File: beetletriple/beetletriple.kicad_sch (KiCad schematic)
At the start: 1 part, among them J1 Power IN

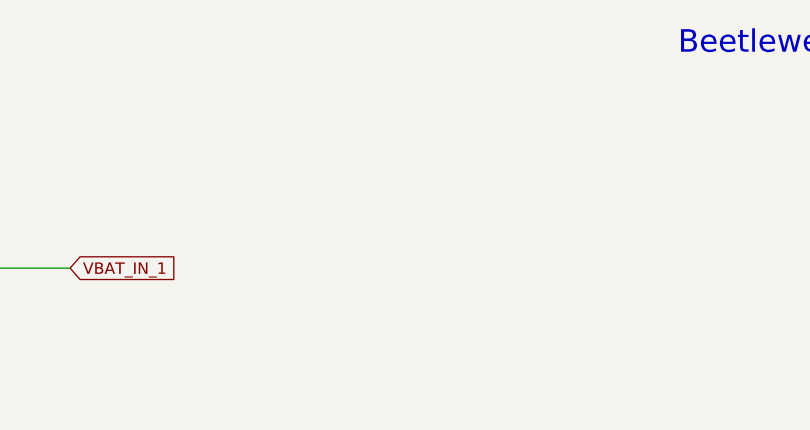
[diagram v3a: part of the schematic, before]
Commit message: Pin swaps and routing
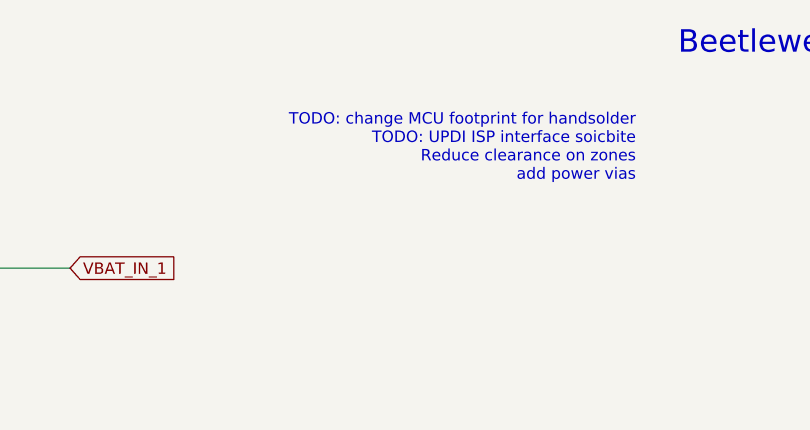
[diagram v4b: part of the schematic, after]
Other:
- note added: "TODO: change MCU footprint for handsolder TODO: UPDI ISP interface soicbite Reduce clearance on zones add power vias"
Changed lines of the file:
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@@
     (stroke (width 0) (type solid) (color 0 0 0 0))
+  )
+  (text "TODO: change MCU footprint for handsolder\nTODO: UPDI ISP interface soicbite\nReduce clearance on zones\nadd power vias "
+    (at 109.22 43.815 0)
+    (effects (font (size 1.27 1.27)) (justify right bottom))
   )
   (text "Beetleweight triple ESC" (at 154.305 29.845 180)
@@
       (reference "J1") (unit 1) (value "Power IN") (footprint "TerminalBlock:TerminalBlock_Wuerth_691311400102_P7.62mm")
     )
+    (path "/6d93a432-011d-4d1d-9c43-a648615a7ea3/22d9c911-bea7-4fc4-93b7-a8a13fd1aa13"
+      (reference "#FLG0101") (unit 1) (value "PWR_FLAG") (footprint "")
+    )
+    (path "/6d93a432-011d-4d1d-9c43-a648615a7ea3/75b3d201-a388-4172-8517-0aab374793dc"
+      (reference "#FLG0102") (unit 1) (value "PWR_FLAG") (footprint "")
+    )
+    (path "/6d93a432-011d-4d1d-9c43-a648615a7ea3/b538e895-f3c3-446e-9001-2df4142c87bf"
+      (reference "#FLG?") (unit 1) (value "PWR_FLAG") (footprint "")
+    )
     (path "/6d93a432-011d-4d1d-9c43-a648615a7ea3/60cf72a3-da49-4391-a543-e025e0f19f60"

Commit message: Add new power in connector
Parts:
- J1: footprint TerminalBlock:TerminalBlock_Wuerth_691311400102_P7.62mm -> beetletriple:beetlepower
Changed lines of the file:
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@@
     (property "Reference" "J1" (id 0) (at 27.4574 47.7582 0))
     (property "Value" "Power IN" (id 1) (at 27.4574 50.0569 0))
-    (property "Footprint" "TerminalBlock:TerminalBlock_Wuerth_691311400102_P7.62mm" (id 2) (at 24.765 55.88 0)
+    (property "Footprint" "beetletriple:beetlepower" (id 2) (at 24.765 55.88 0)
       (effects (font (size 1.27 1.27)) hide)
     )
@@
     )
     (path "/9e85b9a1-64a3-43d7-a600-53fc362386e6"
-      (reference "J1") (unit 1) (value "Power IN") (footprint "TerminalBlock:TerminalBlock_Wuerth_691311400102_P7.62mm")
+      (reference "J1") (unit 1) (value "Power IN") (footprint "beetletriple:beetlepower")
     )
     (path "/6d93a432-011d-4d1d-9c43-a648615a7ea3/22d9c911-bea7-4fc4-93b7-a8a13fd1aa13"

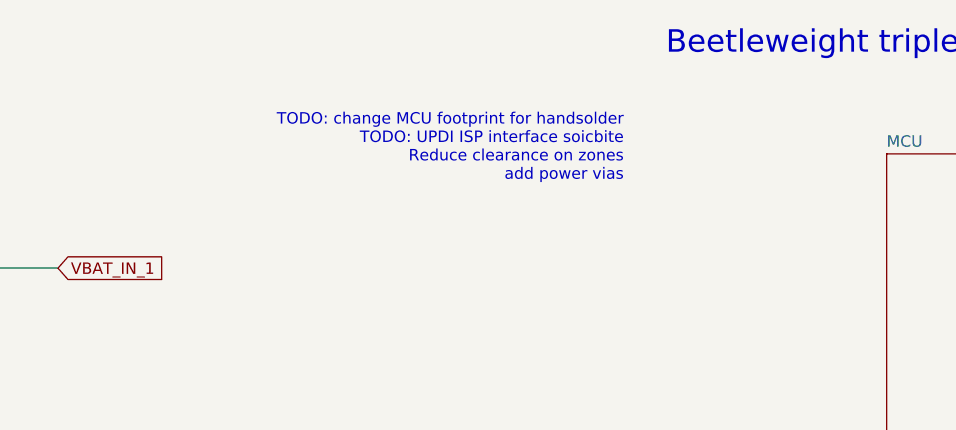
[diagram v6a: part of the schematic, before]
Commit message: Shunt current sensor. Many improvements, layout updates
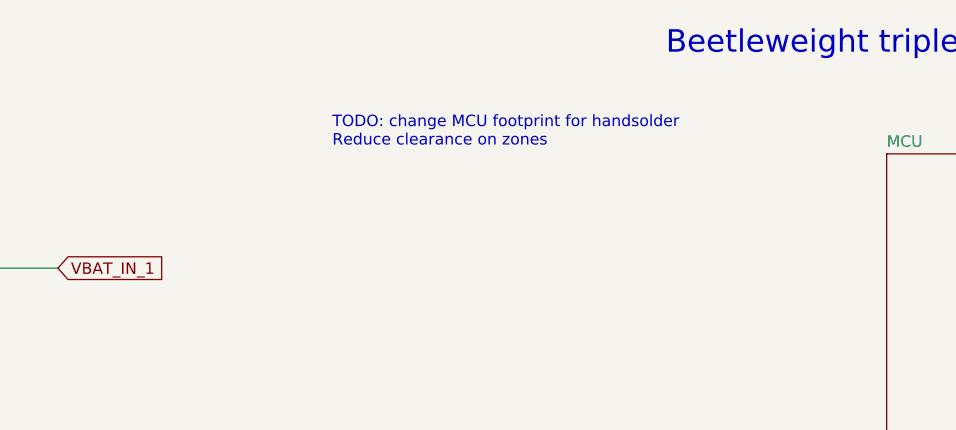
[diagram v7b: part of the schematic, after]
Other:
- note added: "TODO: change MCU footprint for handsolder Reduce clearance on zones"
- note removed: "TODO: change MCU footprint for handsolder TODO: UPDI ISP interface soicbite Reduce clearance on zones add power vias"
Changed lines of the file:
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@@
     (stroke (width 0) (type solid) (color 0 0 0 0))
   )
-  (text "TODO: change MCU footprint for handsolder\nTODO: UPDI ISP interface soicbite\nReduce clearance on zones\nadd power vias "
-    (at 109.22 43.815 0)
-    (effects (font (size 1.27 1.27)) (justify right bottom))
+  (text "TODO: change MCU footprint for handsolder\nReduce clearance on zones\n"
+    (at 76.835 40.005 0)
+    (effects (font (size 1.27 1.27)) (justify left bottom))
   )
   (text "Beetleweight triple ESC" (at 154.305 29.845 180)
@@
     )
     (path "/6d93a432-011d-4d1d-9c43-a648615a7ea3/f69d8565-9cce-4269-8146-6fce66bbe553"
-      (reference "F1") (unit 1) (value "20mmx5 fuse holder") (footprint "Fuse:Fuseholder_Cylinder-5x20mm_Schurter_0031_8201_Horizontal_Open")
+      (reference "F1") (unit 1) (value "20mmx5 fuse holder") (footprint "beetletriple:fuseholder_flexible")
     )
     (path "/6d93a432-011d-4d1d-9c43-a648615a7ea3/867e4d9b-1a41-4ccb-b503-ce8c72df462b"
@@
       (reference "U3") (unit 1) (value "ATtiny1617-M") (footprint "Package_DFN_QFN:QFN-24-1EP_4x4mm_P0.5mm_EP2.6x2.6mm")
     )
-    (path "/88009e22-8327-4e67-a142-0e1ef6c68b73/e804135f-e8f0-42d8-b72d-8d477eea7a6a"
-      (reference "#PWR08") (unit 1) (value "GND") (footprint "")
-    )
     (path "/88009e22-8327-4e67-a142-0e1ef6c68b73/ab274dd8-db81-4ae2-8ed3-2c7949792599"
       (reference "#PWR09") (unit 1) (value "GND") (footprint "")
     )
-    (path "/88009e22-8327-4e67-a142-0e1ef6c68b73/8070a27d-6474-4b23-9f06-b70c2cbe7c4c"
-      (reference "#PWR010") (unit 1) (value "GND") (footprint "")
-    )
     (path "/88009e22-8327-4e67-a142-0e1ef6c68b73/8dbc2066-8818-450a-aceb-6c7ded2cdcb6"
       (reference "#PWR011") (unit 1) (value "GND") (footprint "")
@@
       (reference "R9") (unit 1) (value "4.7R") (footprint "Resistor_SMD:R_0805_2012Metric")
     )
+    (path "/88009e22-8327-4e67-a142-0e1ef6c68b73/796335aa-e3db-4898-a68a-1d6c311d3e51"
+      (reference "R16") (unit 1) (value "0.01R shunt") (footprint "Resistor_SMD:R_2512_6332Metric_Pad1.40x3.35mm_HandSolder")
+    )
+    (path "/88009e22-8327-4e67-a142-0e1ef6c68b73/e1ca83c5-e194-4d52-9886-f3b449d8949e"
+      (reference "R17") (unit 1) (value "0.01R shunt") (footprint "Resistor_SMD:R_2512_6332Metric_Pad1.40x3.35mm_HandSolder")
+    )
+    (path "/88009e22-8327-4e67-a142-0e1ef6c68b73/7fed0b49-b4ef-4fd7-a32f-53cd92b161a3"
+      (reference "R18") (unit 1) (value "1.5k") (footprint "Resistor_SMD:R_0805_2012Metric")
+    )
     (path "/88009e22-8327-4e67-a142-0e1ef6c68b73/2b35b0a5-5087-4576-935a-95c4340d99d1"
